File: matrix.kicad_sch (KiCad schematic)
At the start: 37 parts, among them SW1 EC_SW, SW10 EC_SW, SW11 EC_SW, SW12 EC_SW, SW13 EC_SW, SW14 EC_SW, SW15 EC_SW, SW16 EC_SW, SW17 EC_SW, SW18 EC_SW, SW19 EC_SW, SW2 EC_SW, SW20 EC_SW, SW21 EC_SW, SW22 EC_SW, SW23 EC_SW, SW24 EC_SW, SW25 EC_SW, SW26 EC_SW, SW27 EC_SW, SW28 EC_SW, SW29 EC_SW, SW3 EC_SW, SW30 EC_SW, SW31 EC_SW, SW32 EC_SW, SW33 EC_SW, SW34 EC_SW, SW35 EC_SW, SW36 EC_SW, SW37 EC_SW, SW4 EC_SW, SW5 EC_SW, SW6 EC_SW, SW7 EC_SW, SW8 EC_SW, SW9 EC_SW

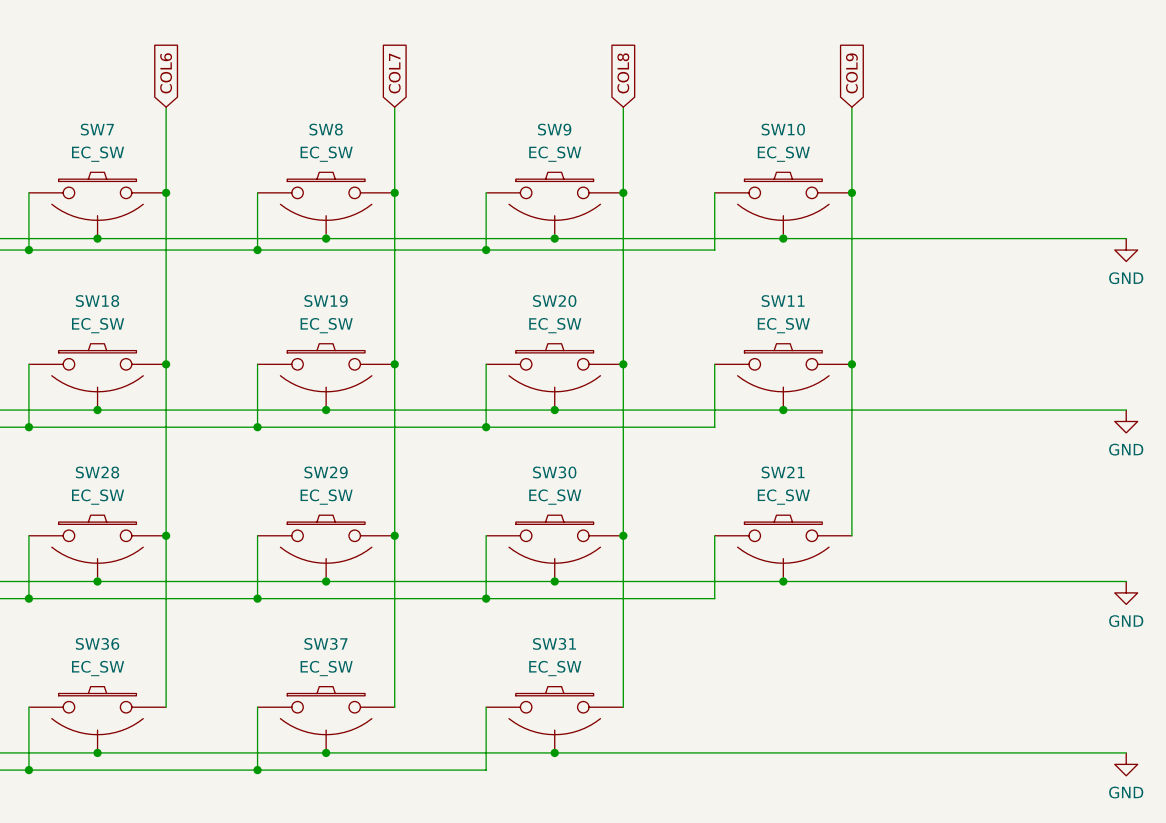
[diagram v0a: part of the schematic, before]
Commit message: one pin matrix fix
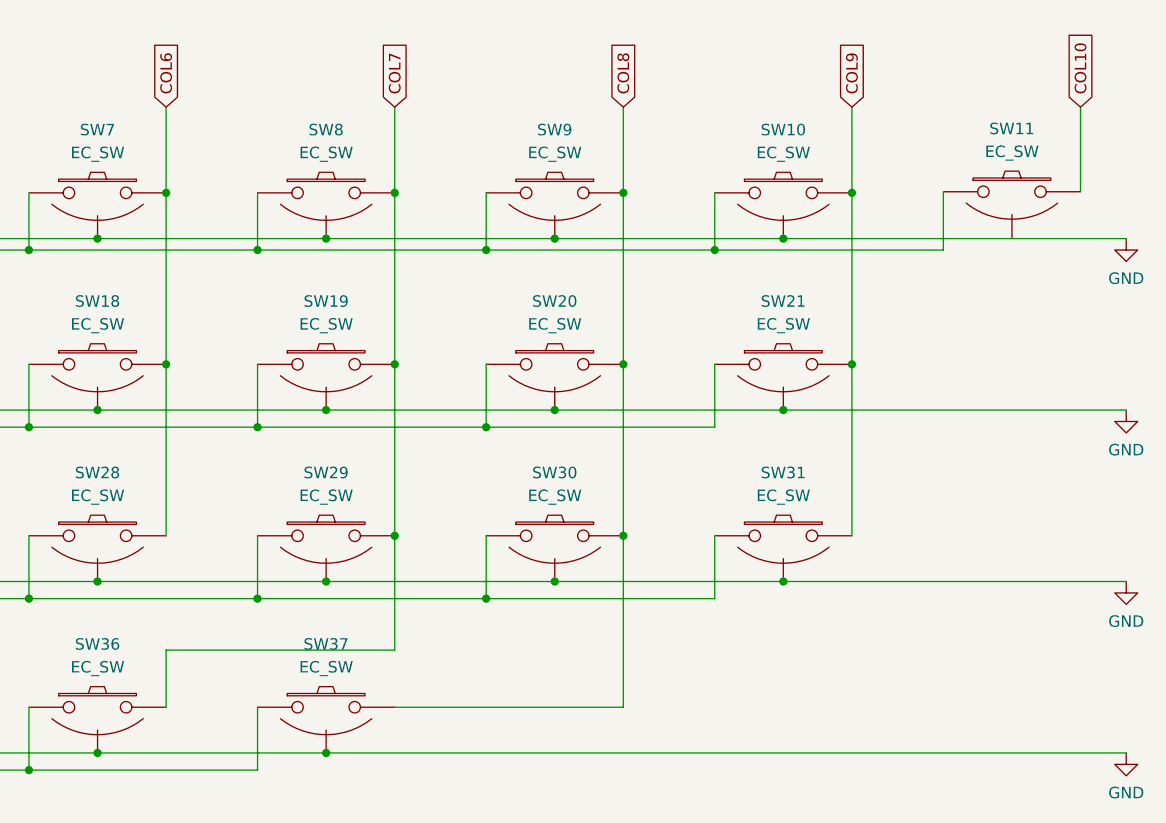
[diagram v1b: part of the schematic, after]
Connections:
- net COL6: no longer SW36.2
- net COL7: now also SW36.2; no longer SW37.2
- net COL8: now also SW37.2; no longer SW31.2
- net COL9: now also SW31.2; no longer SW11.2
- net GND: no longer SW11.3 (SG)
- net ROW0: now also SW11.1
- net ROW1: now also SW21.1; no longer SW11.1
- net ROW2: now also SW31.1; no longer SW21.1
- net ROW3: no longer SW31.1
- new net COL10: SW11.2
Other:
- moved on the sheet: SW11, SW21, SW31
